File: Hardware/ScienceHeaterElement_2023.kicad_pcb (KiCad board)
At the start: 2 copper layers, 50.8 x 38.1 mm, 12 parts, among them Q1 Si4162DY, U1 LMT85DCK

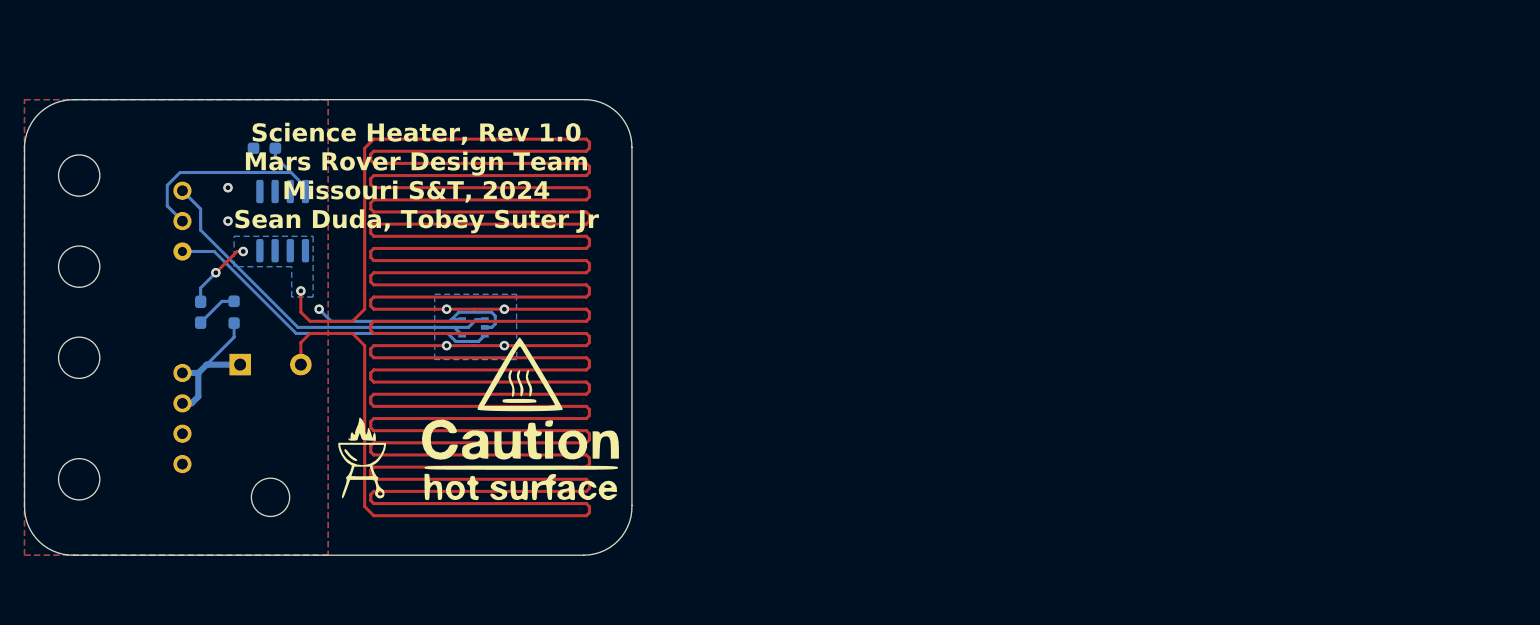
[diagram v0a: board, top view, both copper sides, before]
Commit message: Add back mounting holes and regenerate Gerbs
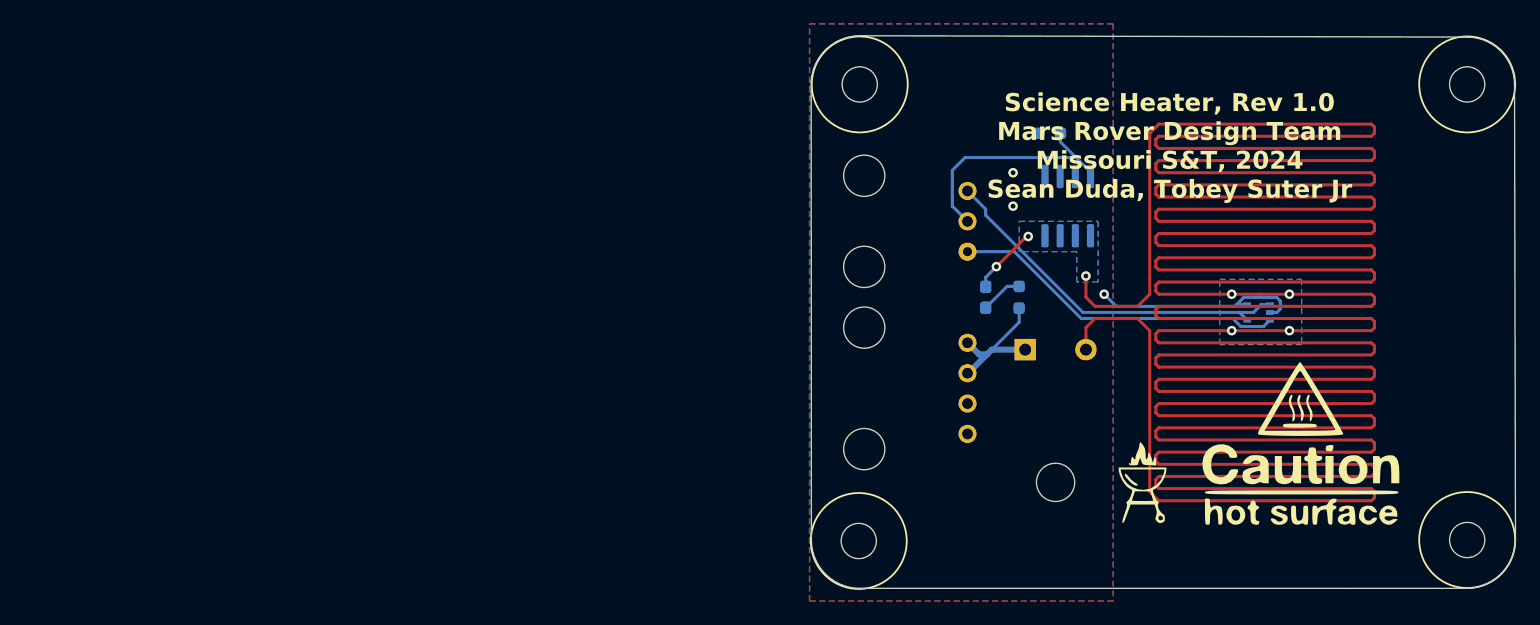
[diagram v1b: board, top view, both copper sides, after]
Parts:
- added REF**: 4_40_Hole, MRDT_Drill_Holes:4_40_Hole_Corner, F.Cu at (130.9, 64.7)
- added REF**: 4_40_Hole, MRDT_Drill_Holes:4_40_Hole_Corner, F.Cu at (173.8, 34.5)
- added REF**: 4_40_Hole, MRDT_Drill_Holes:4_40_Hole_Corner, F.Cu at (173.8, 64.6)
- added REF**: 4_40_Hole, MRDT_Drill_Holes:4_40_Hole_Corner, F.Cu at (131.0, 34.5)
- moved Conn2 65.7 mm to (136.0, 52.1)
- moved G*** 65.7 mm to (157.6, 60.4)
- moved G*** 65.7 mm to (170.8, 63.5)
- moved Q1 65.7 mm to (144.4, 40.7)
- moved R2 65.7 mm to (140.3, 48.3)
- moved R3 65.7 mm to (142.9, 34.6)
- moved U1 65.7 mm to (160.4, 49.5)
- moved D1 65.7 mm to (137.5, 48.3)
- moved R1 65.7 mm to (140.8, 52.7)
- moved Conn1 65.7 mm to (136.0, 39.4)
- moved G*** 65.3 mm to (150.6, 63.5)
- moved G*** 65.3 mm to (163.8, 60.5)
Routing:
- net Gate_Driving_Pin: track 19.0 -> 20.2 mm
- net +3.3V: track 32.4 -> 31.1 mm
- net +12V: track 13.1 -> 12.1 mm
- net Temp_Sense: track 28.6 -> 28.1 mm
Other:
- board size 50.8 x 38.1 mm -> 58.9 x 46.2 mm

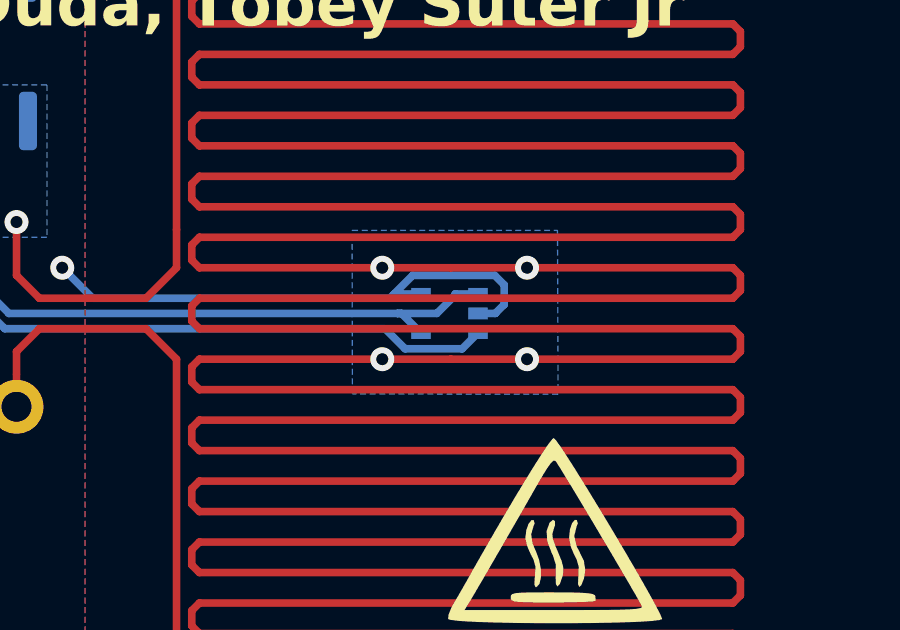
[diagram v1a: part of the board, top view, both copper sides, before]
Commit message: Changed Temp Sensor plane to GND
Changed Temp sensor plane to GND and added GND vias between front and back layers
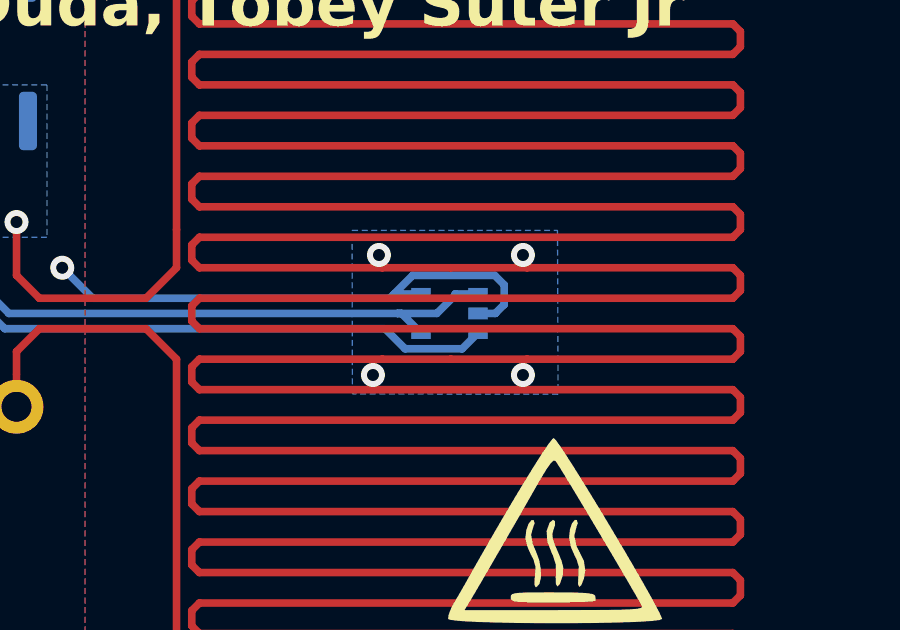
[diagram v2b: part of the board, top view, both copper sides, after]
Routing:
- net GND: vias 3 -> 7
- net /Heater_Trace: vias 7 -> 3
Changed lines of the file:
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@@
   (gr_line (start 170.42925 33.67375) (end 151.37925 33.67375)
     (stroke (width 0.15) (type default)) (layer "Dwgs.User"))
+  (gr_line (start 151.37925 65.42375) (end 151 65.42375)
+    (stroke (width 0.15) (type default)) (layer "Dwgs.User"))
   (gr_line (start 170.42925 65.42375) (end 170.42925 33.67375)
     (stroke (width 0.15) (type default)) (layer "Dwgs.User"))
   (gr_line (start 151.37925 65.42375) (end 170.42925 65.42375)
     (stroke (width 0.15) (type default)) (layer "Dwgs.User"))
-  (gr_line (start 151.37925 33.67375) (end 151.37925 65.42375)
+  (gr_line (start 151 33.67375) (end 151 65.42375)
+    (stroke (width 0.15) (type default)) (layer "Dwgs.User"))
+  (gr_line (start 151 33.67375) (end 151.37925 33.67375)
     (stroke (width 0.15) (type default)) (layer "Dwgs.User"))
   (gr_line (start 177.800001 26.52) (end 127.020562 26.408176)
@@
     (pts (xy 180.34 33.67375) (xy 180.34 65.42375))
     (height 0)
-    (gr_text "1250.0000 mils" (at 179.19 49.54875 90) (layer "Dwgs.User")
+    (gr_text "1.2500 in" (at 179.19 49.54875 90) (layer "Dwgs.User")
       (effects (font (size 1 1) (thickness 0.15)))
     )
@@
     (pts (xy 177.8 68.59875) (xy 177.8 65.42375))
     (height 2.54)
-    (gr_text "125.0000 mils" (at 179.19 67.01125 90) (layer "Dwgs.User")
+    (gr_text "0.1250 in" (at 179.19 67.01125 90) (layer "Dwgs.User")
       (effects (font (size 1 1) (thickness 0.15)))
     )
@@
     (pts (xy 173.355 72.39) (xy 170.18 72.39))
     (height -2.54)
-    (gr_text "125.0000 mils" (at 171.7675 73.78) (layer "Dwgs.User")
+    (gr_text "0.1250 in" (at 171.7675 73.78) (layer "Dwgs.User")
       (effects (font (size 1 1) (thickness 0.15)))
     )
@@
     (pts (xy 122.80425 30.49875) (xy 122.80425 68.59875))
     (height 6.349999)
-    (gr_text "1500.0000 mils" (at 115.304251 49.54875 90) (layer "Dwgs.User")
+    (gr_text "1.5000 in" (at 115.304251 49.54875 90) (layer "Dwgs.User")
       (effects (font (size 1 1) (thickness 0.15)))
     )
@@
     (pts (xy 151.13 74.93) (xy 170.18 74.93))
     (height 0)
-    (gr_text "750.0000 mils" (at 160.655 73.78) (layer "Dwgs.User")
+    (gr_text "0.7500 in" (at 160.655 73.78) (layer "Dwgs.User")
       (effects (font (size 1 1) (thickness 0.15)))
     )
@@
     (pts (xy 177.8 30.49875) (xy 177.8 33.67375))
     (height -2.54)
-    (gr_text "125.0000 mils" (at 179.19 32.08625 90) (layer "Dwgs.User")
+    (gr_text "0.1250 in" (at 179.19 32.08625 90) (layer "Dwgs.User")
       (effects (font (size 1 1) (thickness 0.15)))
     )
@@
     (pts (xy 147.955 72.39) (xy 151.13 72.39))
     (height 2.54)
-    (gr_text "125.0000 mils" (at 149.5425 73.78) (layer "Dwgs.User")
+    (gr_text "0.1250 in" (at 149.5425 73.78) (layer "Dwgs.User")
       (effects (font (size 1 1) (thickness 0.15)))
     )
@@
     (pts (xy 173.60425 30.49875) (xy 148.20425 30.49875))
     (height 2.539999)
-    (gr_text "1000.0000 mils" (at 160.90425 26.808751) (layer "Dwgs.User")
+    (gr_text "1.0000 in" (at 160.90425 26.808751) (layer "Dwgs.User")
       (effects (font (size 1 1) (thickness 0.15)))
     )
@@
     (pts (xy 126.99492 30.47492) (xy 177.80508 30.47492))
     (height -6.35)
-    (gr_text "2000.4000 mils" (at 152.4 22.97492) (layer "Dwgs.User")
+    (gr_text "2.0004 in" (at 152.4 22.97492) (layer "Dwgs.User")
       (effects (font (size 1 1) (thickness 0.15)))
     )
@@
   (segment (start 160.53825 48.94023) (end 159.92973 49.54875) (width 0.254) (layer "B.Cu") (net 1))
   (segment (start 137.53625 41.423578) (end 137.53625 41.42075) (width 0.254) (layer "B.Cu") (net 1))
+  (via (at 157.8 51.6) (size 0.8) (drill 0.4) (layers "F.Cu" "B.Cu") (free) (net 2))
+  (via (at 162.8 47.6) (size 0.8) (drill 0.4) (layers "F.Cu" "B.Cu") (free) (net 2))
   (via (at 139.82225 40.65875) (size 0.8) (drill 0.4) (layers "F.Cu" "B.Cu") (free) (net 2))
+  (via (at 162.8 51.6) (size 0.8) (drill 0.4) (layers "F.Cu" "B.Cu") (free) (net 2))
+  (via (at 158 47.6) (size 0.8) (drill 0.4) (layers "F.Cu" "B.Cu") (free) (net 2))
   (via (at 139.82225 37.86475) (size 0.8) (drill 0.4) (layers "F.Cu" "B.Cu") (free) (net 2))
   (via (at 147.44225 48.02475) (size 0.8) (drill 0.4) (layers "F.Cu" "B.Cu") (free) (net 2))
@@
   (segment (start 151.76025 61.48675) (end 151.76025 61.99475) (width 0.254) (layer "F.Cu") (net 5))
   (segment (start 145.91825 52.65875) (end 145.91825 51.58075) (width 0.25) (layer "F.Cu") (net 5))
-  (via (at 158.11025 48.02475) (size 0.8) (drill 0.4) (layers "F.Cu" "B.Cu") (net 5))
-  (via (at 158.11025 51.07275) (size 0.8) (drill 0.4) (layers "F.Cu" "B.Cu") (net 5))
   (via (at 145.91825 46.50075) (size 0.8) (drill 0.4) (layers "F.Cu" "B.Cu") (net 5))
-  (via (at 162.93625 51.07275) (size 0.8) (drill 0.4) (layers "F.Cu" "B.Cu") (net 5))
-  (via (at 162.93625 48.02475) (size 0.8) (drill 0.4) (layers "F.Cu" "B.Cu") (net 5))
   (via (at 138.43 45.72) (size 0.8) (drill 0.4) (layers "F.Cu" "B.Cu") (net 5))
   (via (at 141.09225 43.19875) (size 0.8) (drill 0.4) (layers "F.Cu" "B.Cu") (net 5))
@@
     )
   )
-  (zone (net 5) (net_name "/Heater_Trace") (layer "B.Cu") (name "Heater") (hatch edge 0.5)
+  (zone (net 2) (net_name "GND") (layer "B.Cu") (name "Heater") (hatch edge 0.5)
     (connect_pads (clearance 0))
     (min_thickness 0.25) (filled_areas_thickness no)

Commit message: Expanded GND plane past heater trace area
Extended GND plane past heater trace area and fixed GND island by connecting GND of temp sensor to GND plane properly
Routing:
- net GND: vias 7 -> 18
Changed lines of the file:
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@@
     (pts (xy 180.34 33.67375) (xy 180.34 65.42375))
     (height 0)
-    (gr_text "1.2500 in" (at 179.19 49.54875 90) (layer "Dwgs.User")
+    (gr_text "1250.0000 mils" (at 179.19 49.54875 90) (layer "Dwgs.User")
       (effects (font (size 1 1) (thickness 0.15)))
     )
@@
     (pts (xy 177.8 68.59875) (xy 177.8 65.42375))
     (height 2.54)
-    (gr_text "0.1250 in" (at 179.19 67.01125 90) (layer "Dwgs.User")
+    (gr_text "125.0000 mils" (at 179.19 67.01125 90) (layer "Dwgs.User")
       (effects (font (size 1 1) (thickness 0.15)))
     )
@@
     (pts (xy 173.355 72.39) (xy 170.18 72.39))
     (height -2.54)
-    (gr_text "0.1250 in" (at 171.7675 73.78) (layer "Dwgs.User")
+    (gr_text "125.0000 mils" (at 171.7675 73.78) (layer "Dwgs.User")
       (effects (font (size 1 1) (thickness 0.15)))
     )
@@
     (pts (xy 122.80425 30.49875) (xy 122.80425 68.59875))
     (height 6.349999)
-    (gr_text "1.5000 in" (at 115.304251 49.54875 90) (layer "Dwgs.User")
+    (gr_text "1500.0000 mils" (at 115.304251 49.54875 90) (layer "Dwgs.User")
       (effects (font (size 1 1) (thickness 0.15)))
     )
@@
     (pts (xy 151.13 74.93) (xy 170.18 74.93))
     (height 0)
-    (gr_text "0.7500 in" (at 160.655 73.78) (layer "Dwgs.User")
+    (gr_text "750.0000 mils" (at 160.655 73.78) (layer "Dwgs.User")
       (effects (font (size 1 1) (thickness 0.15)))
     )
@@
     (pts (xy 177.8 30.49875) (xy 177.8 33.67375))
     (height -2.54)
-    (gr_text "0.1250 in" (at 179.19 32.08625 90) (layer "Dwgs.User")
+    (gr_text "125.0000 mils" (at 179.19 32.08625 90) (layer "Dwgs.User")
       (effects (font (size 1 1) (thickness 0.15)))
     )
@@
     (pts (xy 147.955 72.39) (xy 151.13 72.39))
     (height 2.54)
-    (gr_text "0.1250 in" (at 149.5425 73.78) (layer "Dwgs.User")
+    (gr_text "125.0000 mils" (at 149.5425 73.78) (layer "Dwgs.User")
       (effects (font (size 1 1) (thickness 0.15)))
     )
@@
     (pts (xy 173.60425 30.49875) (xy 148.20425 30.49875))
     (height 2.539999)
-    (gr_text "1.0000 in" (at 160.90425 26.808751) (layer "Dwgs.User")
+    (gr_text "1000.0000 mils" (at 160.90425 26.808751) (layer "Dwgs.User")
       (effects (font (size 1 1) (thickness 0.15)))
     )
@@
     (pts (xy 126.99492 30.47492) (xy 177.80508 30.47492))
     (height -6.35)
-    (gr_text "2.0004 in" (at 152.4 22.97492) (layer "Dwgs.User")
+    (gr_text "2000.4000 mils" (at 152.4 22.97492) (layer "Dwgs.User")
       (effects (font (size 1 1) (thickness 0.15)))
     )
@@
   (segment (start 160.53825 48.94023) (end 159.92973 49.54875) (width 0.254) (layer "B.Cu") (net 1))
   (segment (start 137.53625 41.423578) (end 137.53625 41.42075) (width 0.254) (layer "B.Cu") (net 1))
-  (via (at 157.8 51.6) (size 0.8) (drill 0.4) (layers "F.Cu" "B.Cu") (free) (net 2))
-  (via (at 162.8 47.6) (size 0.8) (drill 0.4) (layers "F.Cu" "B.Cu") (free) (net 2))
+  (via (at 170.31368 47.516682) (size 0.8) (drill 0.4) (layers "F.Cu" "B.Cu") (free) (net 2))
+  (via (at 170.313731 39.388631) (size 0.8) (drill 0.4) (layers "F.Cu" "B.Cu") (free) (net 2))
+  (via (at 170.313677 63.77275) (size 0.8) (drill 0.4) (layers "F.Cu" "B.Cu") (free) (net 2))
+  (via (at 170.313672 35.324744) (size 0.8) (drill 0.4) (layers "F.Cu" "B.Cu") (free) (net 2))
+  (via (at 170.313677 45.48475) (size 0.8) (drill 0.4) (layers "F.Cu" "B.Cu") (free) (net 2))
+  (via (at 170.313671 53.612756) (size 0.8) (drill 0.4) (layers "F.Cu" "B.Cu") (free) (net 2))
+  (via (at 170.313671 41.420744) (size 0.8) (drill 0.4) (layers "F.Cu" "B.Cu") (free) (net 2))
   (via (at 139.82225 40.65875) (size 0.8) (drill 0.4) (layers "F.Cu" "B.Cu") (free) (net 2))
-  (via (at 162.8 51.6) (size 0.8) (drill 0.4) (layers "F.Cu" "B.Cu") (free) (net 2))
-  (via (at 158 47.6) (size 0.8) (drill 0.4) (layers "F.Cu" "B.Cu") (free) (net 2))
+  (via (at 170.313595 51.58077) (size 0.8) (drill 0.4) (layers "F.Cu" "B.Cu") (free) (net 2))
+  (via (at 170.313675 55.644688) (size 0.8) (drill 0.4) (layers "F.Cu" "B.Cu") (free) (net 2))
+  (via (at 170.313713 57.67685) (size 0.8) (drill 0.4) (layers "F.Cu" "B.Cu") (free) (net 2))
+  (via (at 170.313684 49.548678) (size 0.8) (drill 0.4) (layers "F.Cu" "B.Cu") (free) (net 2))
+  (via (at 170.313713 59.70885) (size 0.8) (drill 0.4) (layers "F.Cu" "B.Cu") (free) (net 2))
+  (via (at 170.313675 37.356688) (size 0.8) (drill 0.4) (layers "F.Cu" "B.Cu") (free) (net 2))
+  (via (at 170.313675 61.740688) (size 0.8) (drill 0.4) (layers "F.Cu" "B.Cu") (free) (net 2))
+  (via (at 170.313678 43.45275) (size 0.8) (drill 0.4) (layers "F.Cu" "B.Cu") (free) (net 2))
   (via (at 139.82225 37.86475) (size 0.8) (drill 0.4) (layers "F.Cu" "B.Cu") (free) (net 2))
   (via (at 147.44225 48.02475) (size 0.8) (drill 0.4) (layers "F.Cu" "B.Cu") (free) (net 2))
@@
   (segment (start 139.32375 47.36625) (end 137.53625 49.15375) (width 0.254) (layer "B.Cu") (net 7))
   (segment (start 140.33025 47.36625) (end 139.32375 47.36625) (width 0.254) (layer "B.Cu") (net 7))
+  (zone (net 2) (net_name "GND") (layers "F&B.Cu") (name "Heater") (hatch edge 0.5)
+    (priority 1)
+    (connect_pads yes (clearance 0))
+    (min_thickness 0.25) (filled_areas_thickness no)
+    (fill yes (thermal_gap 0.5) (thermal_bridge_width 0.5))
+    (polygon
+      (pts
+        (xy 150.622 33.528)
+        (xy 170.688 33.528)
+        (xy 170.688 65.786)
+        (xy 150.622 65.786)
+      )
+    )
+  )
   (zone (net 2) (net_name "GND") (layers "F&B.Cu") (hatch edge 0.5)
     (priority 1)
@@
       )
     )
-  )
-  (zone (net 2) (net_name "GND") (layer "B.Cu") (name "Heater") (hatch edge 0.5)
-    (connect_pads (clearance 0))
-    (min_thickness 0.25) (filled_areas_thickness no)
-    (fill yes (thermal_gap 0.5) (thermal_bridge_width 0.5))
-    (polygon
-      (pts
-        (xy 157.10473 46.78075)
-        (xy 163.95073 46.78075)
-        (xy 163.970852 52.24075)
-        (xy 157.11473 52.23075)
-      )
-    )
